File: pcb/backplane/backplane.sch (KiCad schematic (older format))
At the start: 85 parts, among them U2 IFX9201SGAUMA1, U3 IFX9201SGAUMA1, U4 IFX9201SGAUMA1, U5 PREC004SAAN-RC, U6 IFX9201SGAUMA1

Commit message: updates
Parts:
- L1, L2, L3: value 11uH -> 15uH; footprint backplane:P0847SNL -> backplane:6100-150K-RC
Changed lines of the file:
@@
 P 12150 2100
 F 0 "L1" H 12150 2315 50  0000 C CNN
-F 1 "11uH" H 12150 2224 50  0000 C CNN
-F 2 "backplane:P0847SNL" H 12150 2100 50  0001 C CNN
+F 1 "15uH" H 12150 2224 50  0000 C CNN
+F 2 "backplane:6100-150K-RC" H 12150 2100 50  0001 C CNN
 F 3 "~" H 12150 2100 50  0001 C CNN
 	1    12150 2100
@@
 P 16050 2100
 F 0 "L3" H 16050 2315 50  0000 C CNN
-F 1 "11uH" H 16050 2224 50  0000 C CNN
-F 2 "backplane:P0847SNL" H 16050 2100 50  0001 C CNN
+F 1 "15uH" H 16050 2224 50  0000 C CNN
+F 2 "backplane:6100-150K-RC" H 16050 2100 50  0001 C CNN
 F 3 "~" H 16050 2100 50  0001 C CNN
 	1    16050 2100
@@
 P 19950 2100
 F 0 "L2" H 19950 2315 50  0000 C CNN
-F 1 "11uH" H 19950 2224 50  0000 C CNN
-F 2 "backplane:P0847SNL" H 19950 2100 50  0001 C CNN
+F 1 "15uH" H 19950 2224 50  0000 C CNN
+F 2 "backplane:6100-150K-RC" H 19950 2100 50  0001 C CNN
 F 3 "~" H 19950 2100 50  0001 C CNN
 	1    19950 2100

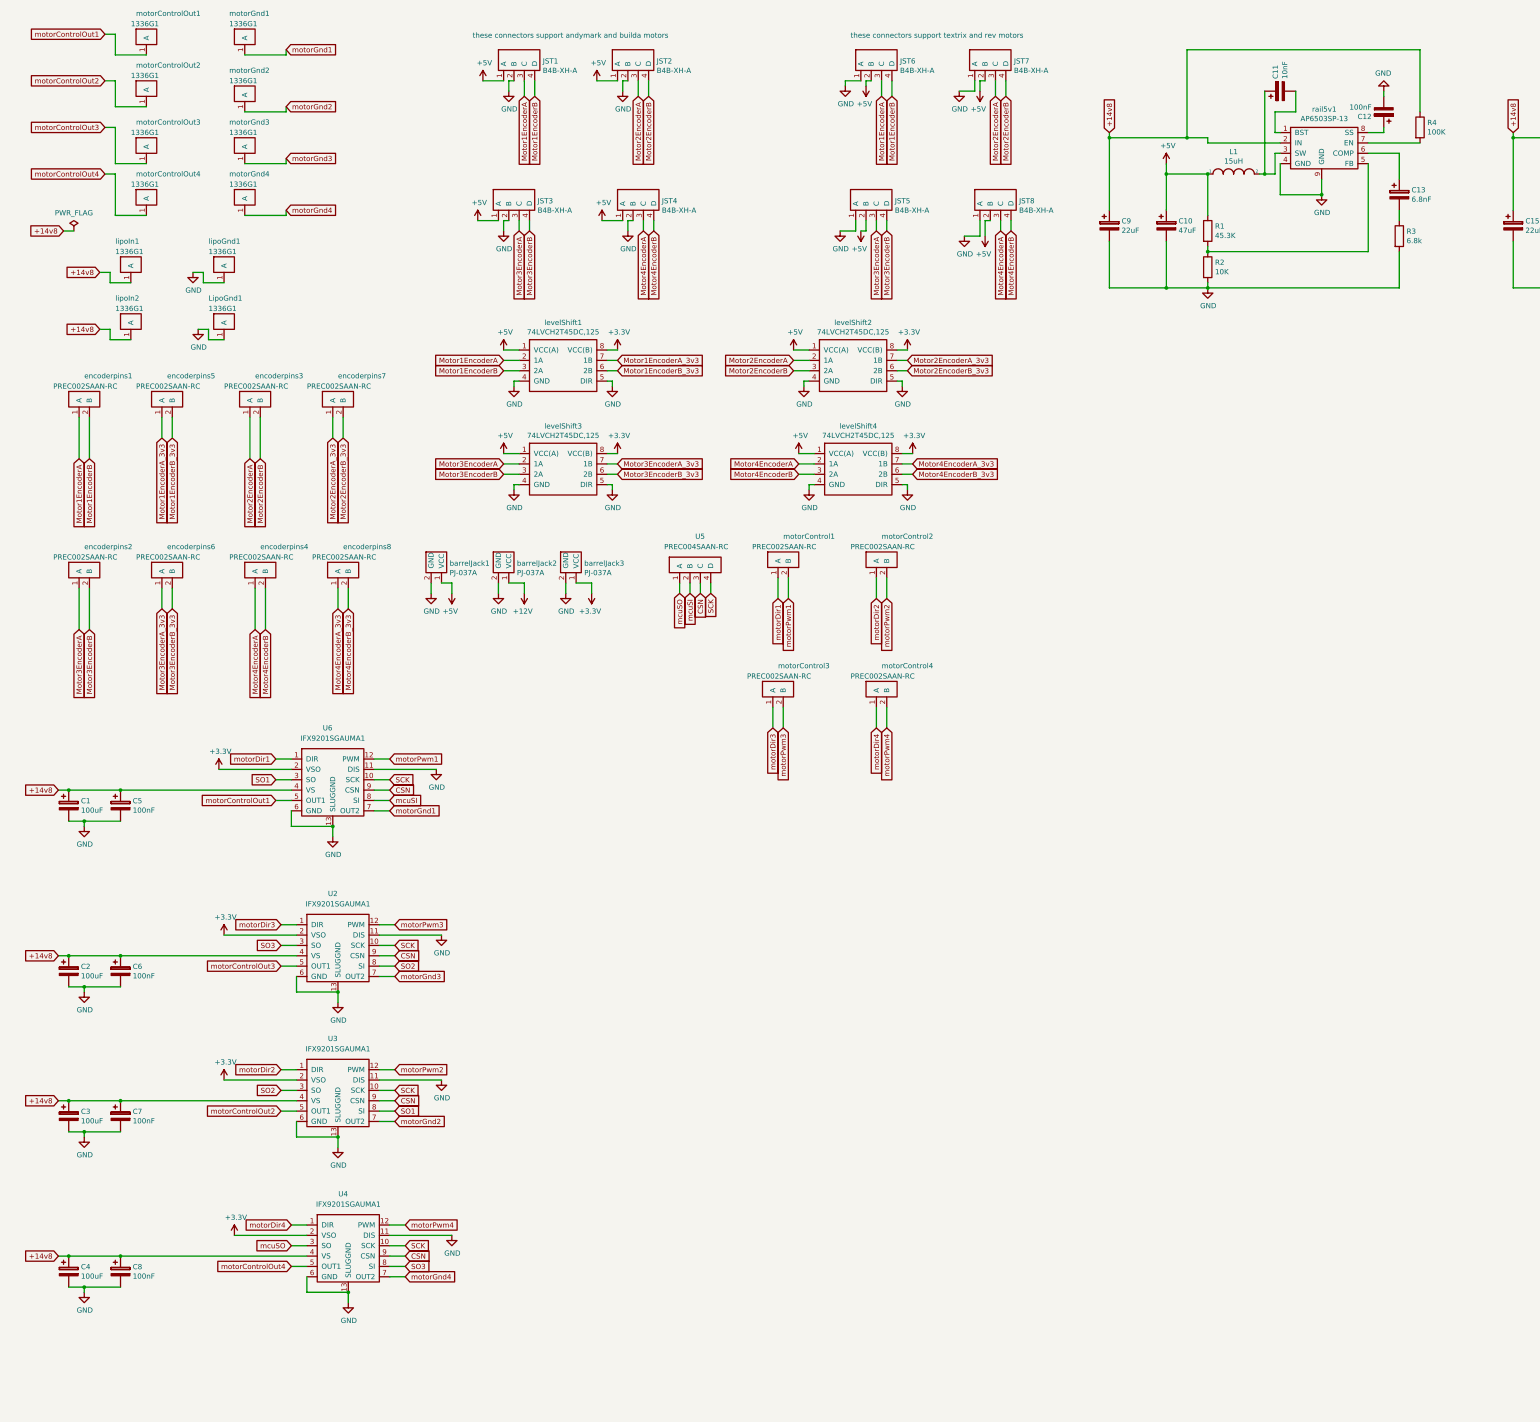
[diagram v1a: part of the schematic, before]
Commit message: updates
finished choosing parts and completed the schematic
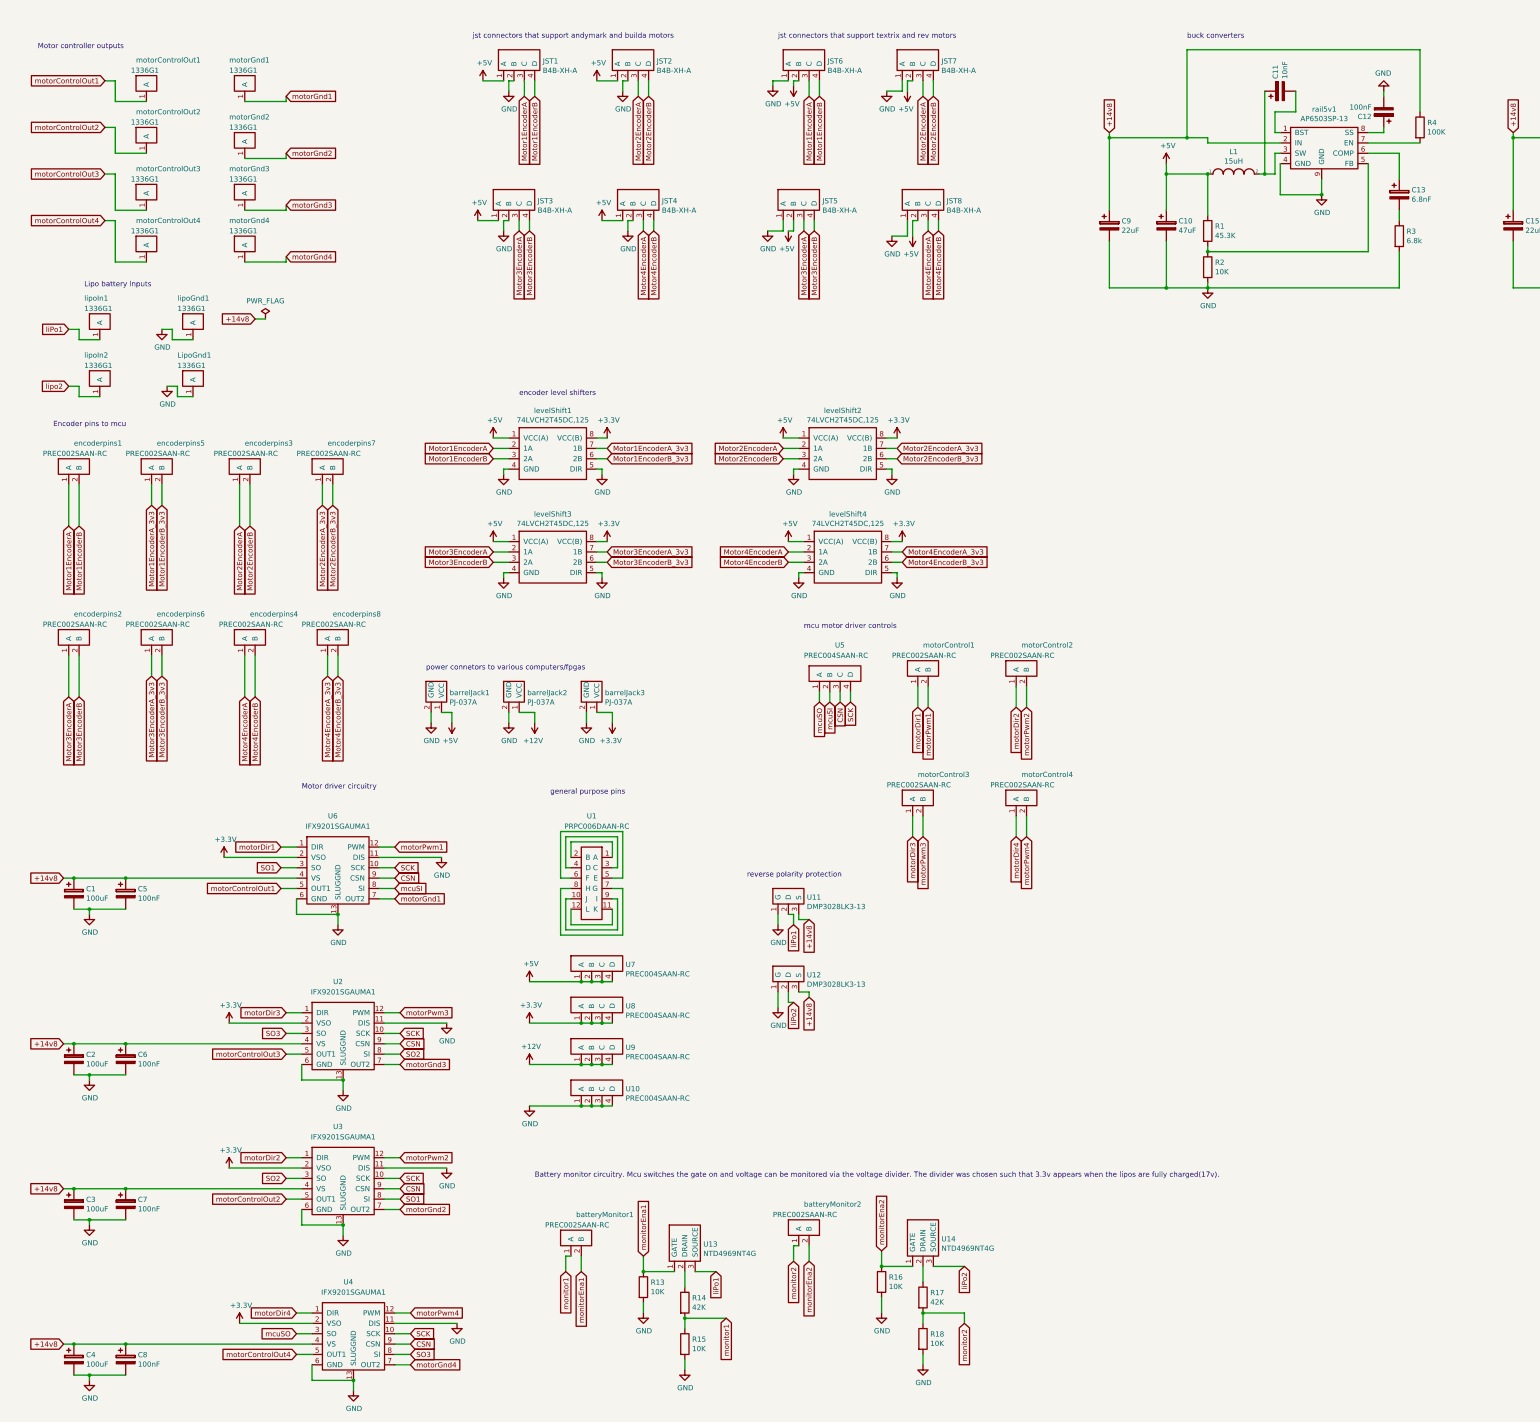
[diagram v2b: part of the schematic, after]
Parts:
- added R13, R15, R16, R18: 10K, Resistor_SMD:R_1206_3216Metric_Pad1.42x1.75mm_HandSolder, symbol Device:R
- added R14, R17: 42K, Resistor_SMD:R_1206_3216Metric_Pad1.42x1.75mm_HandSolder, symbol Device:R
- added U1: PRPC006DAAN-RC, backplane:PRPC006DAAN-RC, symbol backplane_Library:PRPC006DAAN-RC
- added U10, U7, U8, U9: PREC004SAAN-RC, backplane:PREC004SAAN-RC, symbol backplane_Library:PREC004SAAN-RC
- added U11, U12: DMP3028LK3-13, backplane:DMP3028LK3-13, symbol backplane_Library:DMP3028LK3-13
- added U13, U14: NTD4969NT4G, backplane:NTD4969NT4G, symbol backplane_Library:NTD4969NT4G
- added batteryMonitor1, batteryMonitor2: PREC002SAAN-RC, backplane:PREC002SAAN-RC, symbol backplane-rescue:PREC002SAAN-RC-backplane_Library
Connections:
- net +12V: now also U9.1 (A), U9.2 (B), U9.3 (C), U9.4 (D)
- net +14v8: now also U11.3 (S), U12.3 (S); no longer lipoIn1.1 (A), lipoIn2.1 (A)
- net +3V3: now also U8.1 (A), U8.2 (B), U8.3 (C), U8.4 (D)
- net +5V: now also U7.1 (A), U7.2 (B), U7.3 (C), U7.4 (D)
- net GND: now also R13.2, R15.2, R16.2, R18.2, U10.1 (A), U10.2 (B), U10.3 (C), U10.4 (D), U11.1 (G), U12.1 (G)
- new net: U1.1 (A), U1.2 (B)
- new net: U1.10 (J), U1.9 (I)
- new net: U1.11 (K), U1.12 (L)
- new net: U1.3 (C), U1.4 (D)
- new net: U1.5 (E), U1.6 (F)
- new net: U1.7 (G), U1.8 (H)
- new net: R17.1, U14.2 (DRAIN)
- new net: R14.1, U13.2 (DRAIN)
- new net liPo1: U11.2 (D), U13.3 (SOURCE), lipoIn1.1 (A)
- new net liPo2: U12.2 (D), U14.3 (SOURCE)
- new net lipo2: lipoIn2.1 (A)
- new net monitor1: R14.2, R15.1, batteryMonitor1.1 (A)
- new net monitor2: R17.2, R18.1, batteryMonitor2.1 (A)
- new net monitorEna1: R13.1, U13.1 (GATE), batteryMonitor1.2 (B)
- new net monitorEna2: R16.1, U14.1 (GATE), batteryMonitor2.2 (B)
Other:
- note added: "Battery monitor circuitry. Mcu switches the gate on and voltage can be monitored via the voltage divider. The divider was chosen such that 3.3v appears when the lipos are fully charged(17v)."
- note added: "Encoder pins to mcu"
- note added: "Lipo battery inputs\n"
- note added: "Motor controller outputs"
- note added: "Motor driver circuitry\n"
- note added: "buck converters"
- note added: "encoder level shifters"
- note added: "general purpose pins"
- note added: "jst connectors that support andymark and builda motors"
- note added: "jst connectors that support textrix and rev motors"
- note added: "mcu motor driver controls"
- note added: "power connetors to various computers/fpgas"
- note added: "reverse polarity protection"
- note removed: "these connectors support andymark and builda motors"
- note removed: "these connectors support textrix and rev motors"
- moved on the sheet: C1, C2, C3, C4, C5, C6, C7, C8, JST5, JST6, JST7, JST8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

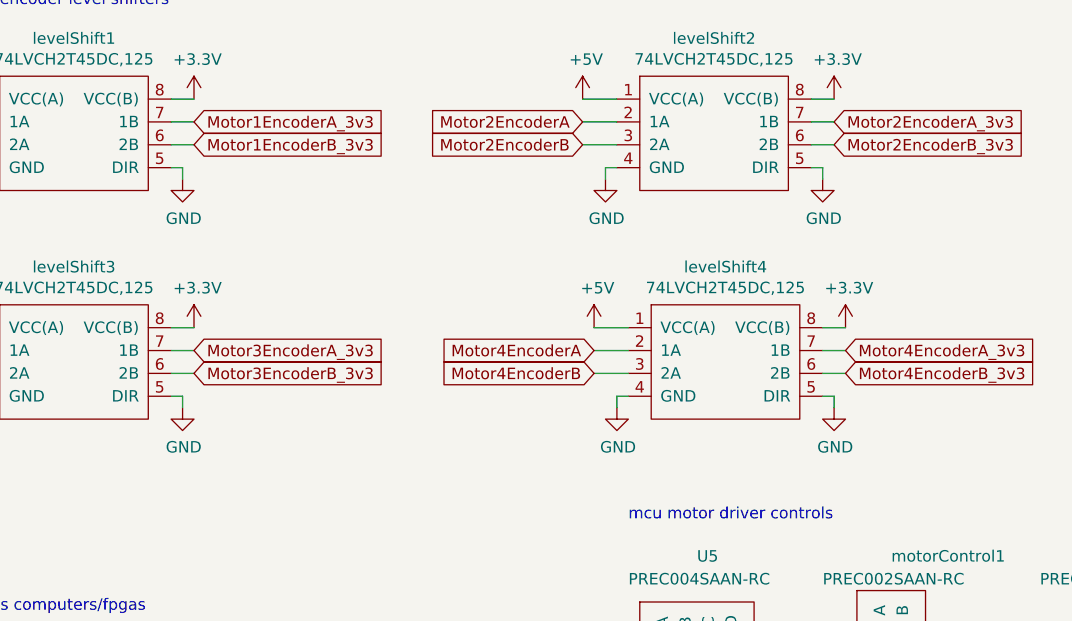
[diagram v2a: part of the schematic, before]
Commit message: changed to a modular design
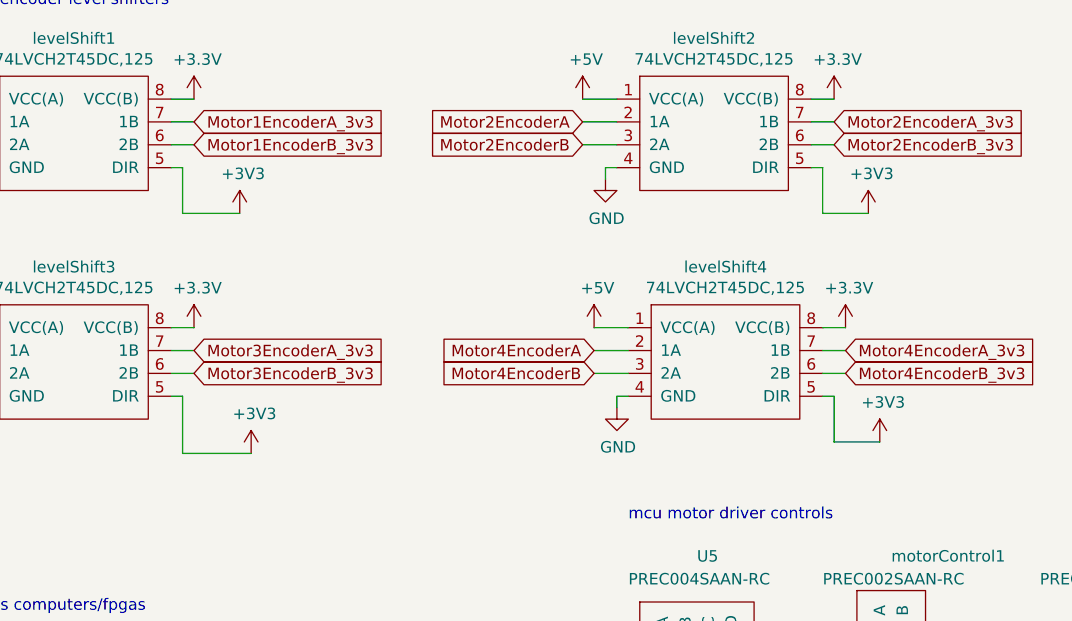
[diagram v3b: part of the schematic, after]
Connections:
- net +3V3: now also levelShift1.5 (DIR), levelShift2.5 (DIR), levelShift3.5 (DIR), levelShift4.5 (DIR)
- net GND: no longer levelShift1.5 (DIR), levelShift2.5 (DIR), levelShift3.5 (DIR), levelShift4.5 (DIR)
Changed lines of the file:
@@
 Wire Wire Line
 	6000 4850 6100 4850
-$Comp
-L power:GND #PWR0104
-U 1 1 5C542F94
-P 6050 5000
-F 0 "#PWR0104" H 6050 4750 50  0001 C CNN
-F 1 "GND" H 6055 4827 50  0000 C CNN
-F 2 "" H 6050 5000 50  0001 C CNN
-F 3 "" H 6050 5000 50  0001 C CNN
-	1    6050 5000
-	1    0    0    -1
-$EndComp
-Wire Wire Line
-	6050 5000 6050 4950
 Wire Wire Line
 	6050 4950 6000 4950
@@
 Wire Wire Line
 	8800 4850 8900 4850
-$Comp
-L power:GND #PWR0108
-U 1 1 5C546A1E
-P 8850 5000
-F 0 "#PWR0108" H 8850 4750 50  0001 C CNN
-F 1 "GND" H 8855 4827 50  0000 C CNN
-F 2 "" H 8850 5000 50  0001 C CNN
-F 3 "" H 8850 5000 50  0001 C CNN
-	1    8850 5000
-	1    0    0    -1
-$EndComp
-Wire Wire Line
-	8850 5000 8850 4950
 Wire Wire Line
 	8850 4950 8800 4950
@@
 Wire Wire Line
 	6000 5850 6100 5850
-$Comp
-L power:GND #PWR0112
-U 1 1 5C54A9A4
-P 6050 6000
-F 0 "#PWR0112" H 6050 5750 50  0001 C CNN
-F 1 "GND" H 6055 5827 50  0000 C CNN
-F 2 "" H 6050 6000 50  0001 C CNN
-F 3 "" H 6050 6000 50  0001 C CNN
-	1    6050 6000
-	1    0    0    -1
-$EndComp
-Wire Wire Line
-	6050 6000 6050 5950
 Wire Wire Line
 	6050 5950 6000 5950
@@
 Wire Wire Line
 	8850 5850 8950 5850
-$Comp
-L power:GND #PWR0116
-U 1 1 5C54F365
-P 8900 6000
-F 0 "#PWR0116" H 8900 5750 50  0001 C CNN
-F 1 "GND" H 8905 5827 50  0000 C CNN
-F 2 "" H 8900 6000 50  0001 C CNN
-F 3 "" H 8900 6000 50  0001 C CNN
-	1    8900 6000
-	1    0    0    -1
-$EndComp
-Wire Wire Line
-	8900 6000 8900 5950
 Wire Wire Line
 	8900 5950 8850 5950
@@
 Text Notes 11700 800  0    50   ~ 0
 buck converters
+$Comp
+L power:+3V3 #PWR?
+U 1 1 5C3FB88E
+P 6350 6200
+F 0 "#PWR?" H 6350 6050 50  0001 C CNN
+F 1 "+3V3" H 6365 6373 50  0000 C CNN
+F 2 "" H 6350 6200 50  0001 C CNN
+F 3 "" H 6350 6200 50  0001 C CNN
+	1    6350 6200
+	1    0    0    -1
+$EndComp
+Wire Wire Line
+	6350 6200 6050 6200
+Wire Wire Line
+	6050 5950 6050 6200
+$Comp
+L power:+3V3 #PWR?
+U 1 1 5C42ACD4
+P 6300 5150
+F 0 "#PWR?" H 6300 5000 50  0001 C CNN
+F 1 "+3V3" H 6315 5323 50  0000 C CNN
+F 2 "" H 6300 5150 50  0001 C CNN
+F 3 "" H 6300 5150 50  0001 C CNN
+	1    6300 5150
+	1    0    0    -1
+$EndComp
+Wire Wire Line
+	6050 5150 6300 5150
+Wire Wire Line
+	6050 4950 6050 5150
+$Comp
+L power:+3V3 #PWR?
+U 1 1 5C45A461
+P 9050 5150
+F 0 "#PWR?" H 9050 5000 50  0001 C CNN
+F 1 "+3V3" H 9065 5323 50  0000 C CNN
+F 2 "" H 9050 5150 50  0001 C CNN
+F 3 "" H 9050 5150 50  0001 C CNN
+	1    9050 5150
+	1    0    0    -1
+$EndComp
+Wire Wire Line
+	8850 5150 9050 5150
+Wire Wire Line
+	8850 4950 8850 5150
+$Comp
+L power:+3V3 #PWR?
+U 1 1 5C48A23F
+P 9100 6150
+F 0 "#PWR?" H 9100 6000 50  0001 C CNN
+F 1 "+3V3" H 9115 6323 50  0000 C CNN
+F 2 "" H 9100 6150 50  0001 C CNN
+F 3 "" H 9100 6150 50  0001 C CNN
+	1    9100 6150
+	1    0    0    -1
+$EndComp
+Wire Wire Line
+	8900 6150 9100 6150
+Wire Wire Line
+	8900 5950 8900 6150
 $EndSCHEMATC
